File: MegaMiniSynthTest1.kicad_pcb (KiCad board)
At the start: 2 copper layers, 73.5 x 56.9 mm, 35 parts, among them K1 CONN_3, P4 DIN_5, U1 MC33269, U2 TLE2426, U3 PCA9685

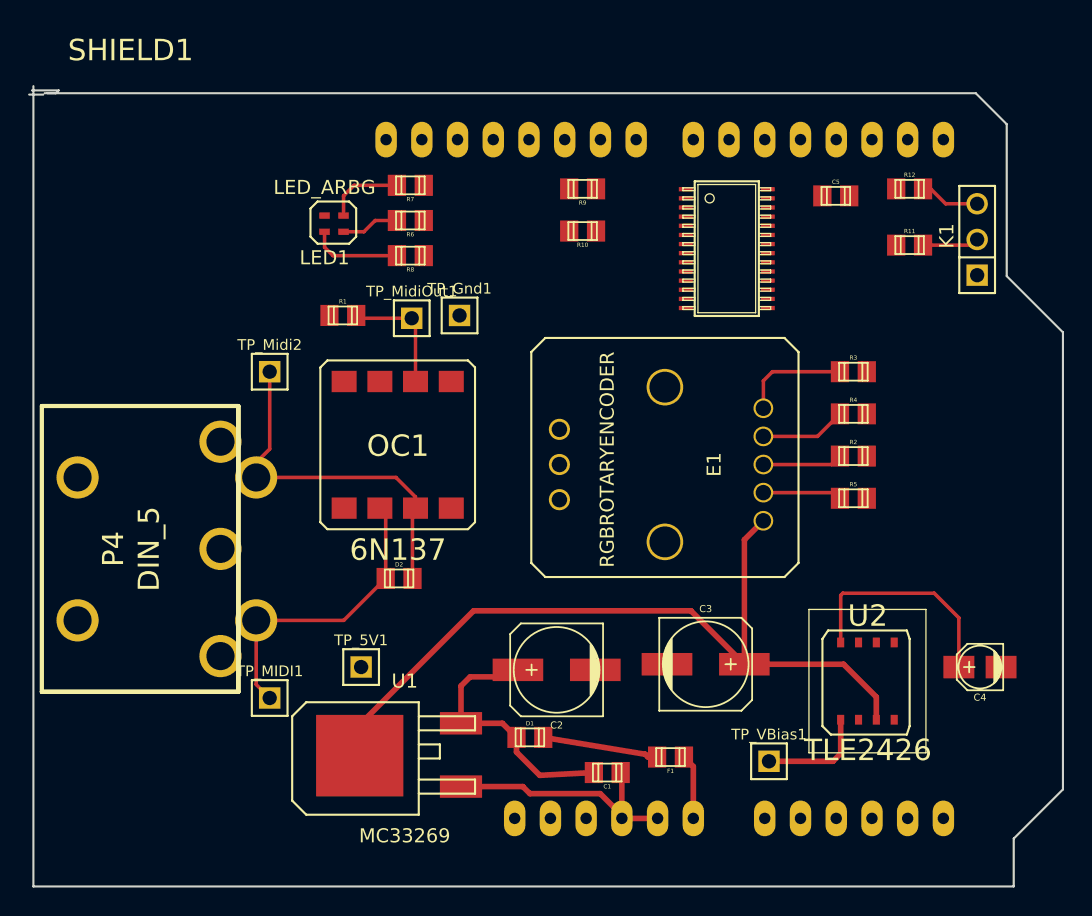
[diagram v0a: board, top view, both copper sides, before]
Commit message: Moved to new KiCad Version
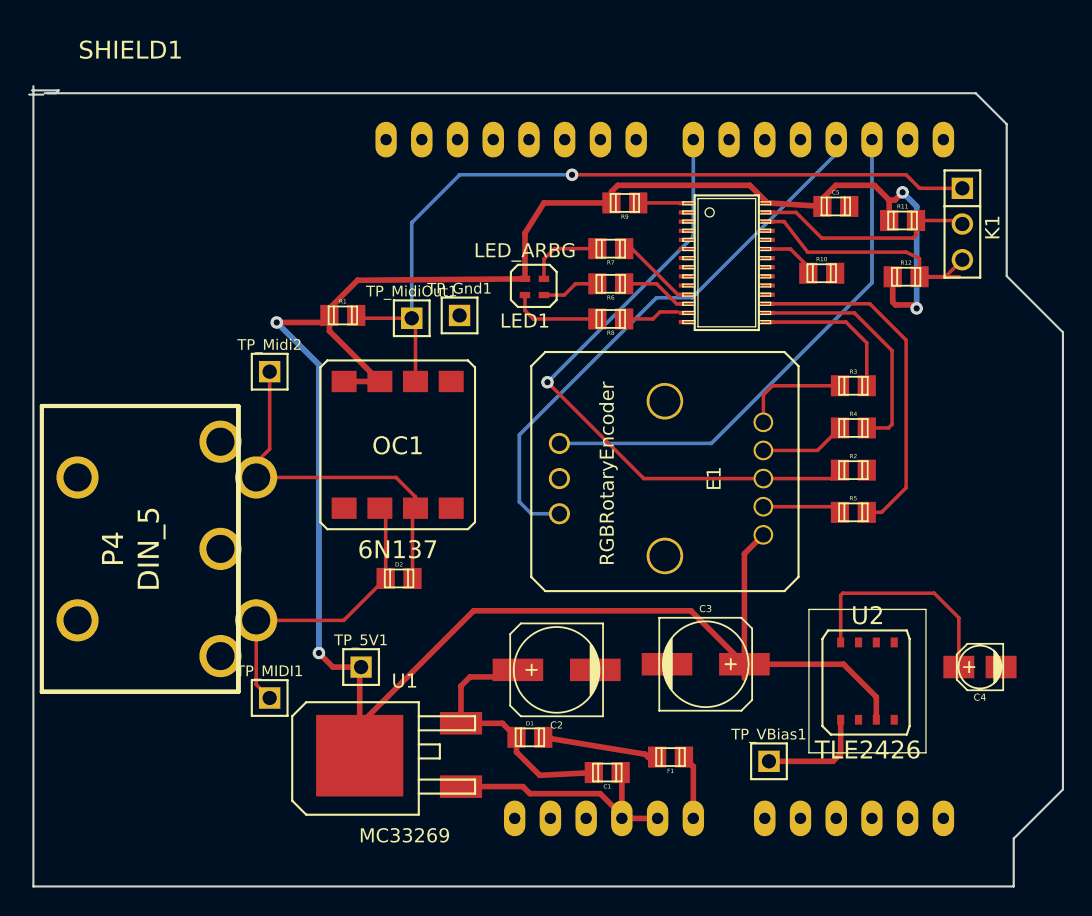
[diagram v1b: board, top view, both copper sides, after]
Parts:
- E1: value RGBROTARYENCODER -> RGBRotaryEncoder
- moved R10 17.3 mm to (134.8, 39.0), turned to 0 degrees
- moved LED1 14.9 mm to (113.7, 39.4)
- moved R6 14.9 mm to (119.8, 39.8)
- moved R7 14.9 mm to (119.8, 37.2)
- moved R8 14.9 mm to (119.8, 42.2)
- moved R12 6.25 mm to (140.8, 39.2)
- moved R9 3.16 mm to (120.8, 34.0)
- moved R11 1.82 mm to (140.5, 35.2)
- moved K1 1.52 mm to (144.8, 35.5), turned to 270 degrees
- moved E1 1.00 mm to (116.1, 53.6)
- moved R2 1.00 mm to (137.0, 53.0)
- moved R3 1.00 mm to (137.0, 47.0)
- moved R4 1.00 mm to (137.0, 50.0)
- moved R5 1.00 mm to (137.0, 56.0)
- moved U3 1.00 mm to (128.0, 38.2)
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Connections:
- P4 pad 1: (no net) -> Net-(P4-Pad1)
- P4 pad 2: (no net) -> Net-(P4-Pad2)
- P4 pad 3: (no net) -> Net-(P4-Pad3)
- R3 pad 1: N-0000027 -> Net-(R3-Pad1)
- R5 pad 1: N-0000029 -> Net-(R5-Pad1)
- R6 pad 2: N-0000020 -> Net-(R6-Pad2)
- R7 pad 2: N-0000021 -> Net-(R7-Pad2)
- SHIELD1 pad 0: (no net) -> Net-(SHIELD1-Pad0)
- SHIELD1 pad 1: (no net) -> Net-(SHIELD1-Pad1)
- SHIELD1 pad 10: (no net) -> Net-(SHIELD1-Pad10)
- SHIELD1 pad 11: (no net) -> Net-(SHIELD1-Pad11)
- SHIELD1 pad 12: (no net) -> Net-(SHIELD1-Pad12)
- SHIELD1 pad 13: (no net) -> Net-(SHIELD1-Pad13)
- SHIELD1 pad 3V3: (no net) -> Net-(SHIELD1-Pad3V3)
- SHIELD1 pad 4: (no net) -> Net-(SHIELD1-Pad4)
- SHIELD1 pad 5: (no net) -> Net-(SHIELD1-Pad5)
- SHIELD1 pad 5V: (no net) -> Net-(SHIELD1-Pad5V)
- SHIELD1 pad 6: (no net) -> Net-(SHIELD1-Pad6)
- SHIELD1 pad 8: (no net) -> Net-(SHIELD1-Pad8)
- SHIELD1 pad 9: (no net) -> Net-(SHIELD1-Pad9)
- SHIELD1 pad AD0: (no net) -> Net-(SHIELD1-PadAD0)
- SHIELD1 pad AD1: (no net) -> Net-(SHIELD1-PadAD1)
- SHIELD1 pad AD2: (no net) -> Net-(SHIELD1-PadAD2)
- SHIELD1 pad AD3: (no net) -> Net-(SHIELD1-PadAD3)
- SHIELD1 pad AD4: (no net) -> Net-(SHIELD1-PadAD4)
- SHIELD1 pad AD5: (no net) -> Net-(SHIELD1-PadAD5)
- SHIELD1 pad AREF: (no net) -> Net-(SHIELD1-PadAREF)
- SHIELD1 pad GND3: (no net) -> Net-(SHIELD1-PadGND3)
- SHIELD1 pad RST: (no net) -> Net-(SHIELD1-PadRST)
- U3 pad 10: (no net) -> Net-(U3-Pad10)
- U3 pad 11: N-0000020 -> Net-(R7-Pad2)
- U3 pad 12: N-0000021 -> Net-(R6-Pad2)
- U3 pad 15: N-0000029 -> Net-(R3-Pad1)
- U3 pad 17: N-0000027 -> Net-(R5-Pad1)
- U3 pad 18: (no net) -> Net-(U3-Pad18)
- U3 pad 19: (no net) -> Net-(U3-Pad19)
- U3 pad 20: (no net) -> Net-(U3-Pad20)
- U3 pad 21: (no net) -> Net-(U3-Pad21)
- U3 pad 22: (no net) -> Net-(U3-Pad22)
- U3 pad 6: (no net) -> Net-(U3-Pad6)
- U3 pad 7: (no net) -> Net-(U3-Pad7)
- U3 pad 8: (no net) -> Net-(U3-Pad8)
- U3 pad 9: (no net) -> Net-(U3-Pad9)
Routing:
- net +5V: track 57.2 -> 167.8 mm, vias 0 -> 4
- net Serial2: track 8.64 -> 56.4 mm, vias 0 -> 1
- net Arduino3: track 0.00 -> 38.8 mm
- net Arduino7: track 5.70 -> 44.4 mm, vias 0 -> 1
- net Arduino2: track 0.00 -> 36.1 mm
- net Net-(R5-Pad1): track 0.00 -> 24.9 mm
- net Net-(R4-Pad1): track 0.00 -> 17.1 mm
- net SCL: track 4.29 -> 19.9 mm
- net SDA: track 4.01 -> 16.2 mm
- net Net-(R3-Pad1): track 0.00 -> 10.7 mm
- net Net-(R7-Pad2): track 0.00 -> 5.74 mm
- net Net-(R6-Pad2): track 0.00 -> 4.97 mm
- net Net-(R8-Pad2): track 0.00 -> 4.00 mm
- net Net-(R10-Pad2): track 0.00 -> 3.86 mm
- net Net-(R9-Pad2): track 0.00 -> 3.39 mm

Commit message: Board Layout basically done
Added bypass cap for PWM driver
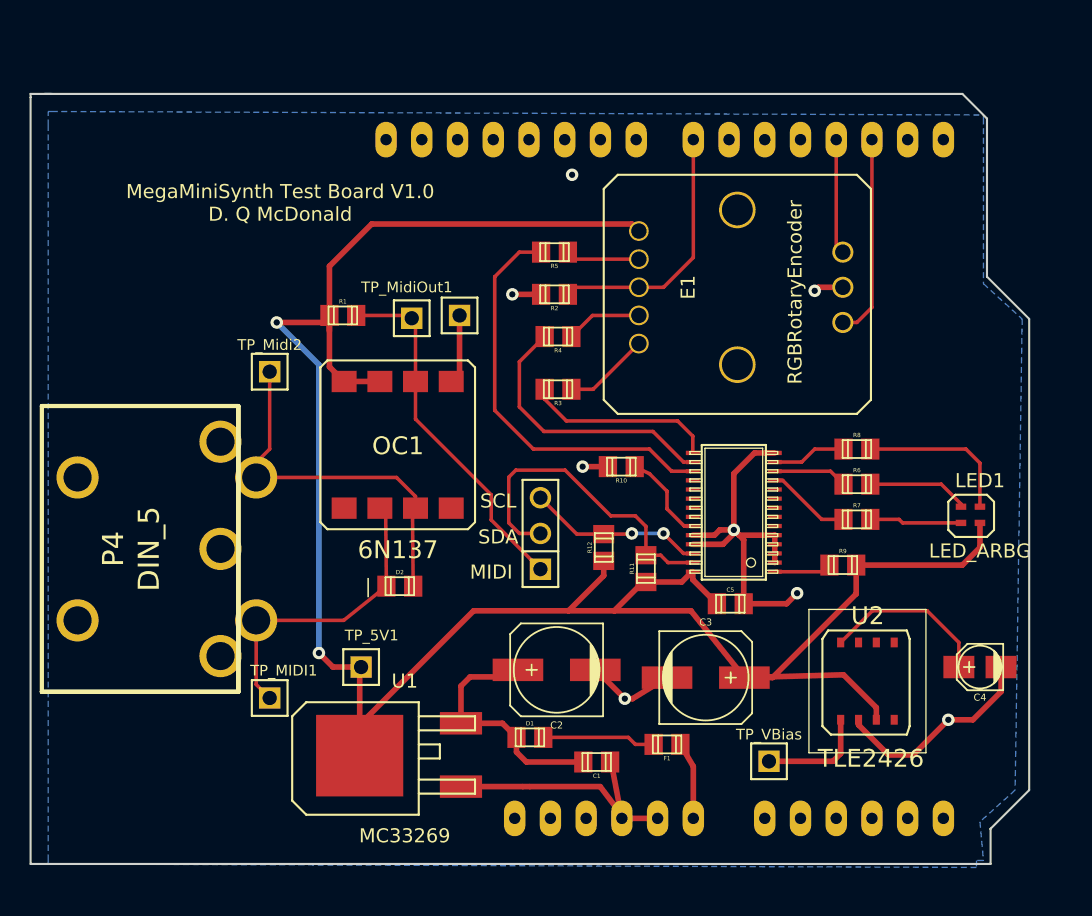
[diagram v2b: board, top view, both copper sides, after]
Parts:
- ?: renamed from SHIELD1; value ARDUINO_SHIELD -> (none)
- ?: renamed from K1; value CONN_3 -> (none)
- TP_5V1: value TP_5V -> (none)
- TP_MIDI1, TP_Midi2, TP_MidiOut1: value CONN_1 -> (none)
- TP_VBias: renamed from TP_VBias1; value Tl_VBias -> (none)
- moved ? 37.2 mm to (114.8, 57.5), turned to 90 degrees
- moved LED1 36.7 mm to (146.0, 56.8), turned to 0 degrees
- moved R11 30.8 mm to (122.2, 60.0), turned to 90 degrees
- moved R9 30.1 mm to (136.2, 59.8), turned to 0 degrees
- moved C5 29.2 mm to (128.2, 62.5)
- moved R12 28.9 mm to (119.2, 58.5), turned to 90 degrees
- moved R5 28.2 mm to (115.8, 37.5), turned to 180 degrees
- moved R7 26.0 mm to (137.2, 56.5), turned to 0 degrees
- moved R2 24.7 mm to (115.8, 40.5), turned to 180 degrees
- moved E1 24.3 mm to (136.2, 40.0), turned to 90 degrees
- moved R6 22.6 mm to (137.2, 54.0), turned to 0 degrees
- moved R4 22.0 mm to (116.0, 43.5), turned to 180 degrees
- moved R3 21.0 mm to (116.0, 47.2), turned to 180 degrees
- moved R10 19.8 mm to (120.5, 52.8), turned to 180 degrees
- moved R8 19.8 mm to (137.2, 51.5), turned to 0 degrees
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- renumbered TP_Gnd1 to ?
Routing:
- net GND: track 18.3 -> 80.6 mm, vias 0 -> 7
- net Serial2: track 56.4 -> 25.9 mm, vias 1 -> 0
- net Arduino3: track 38.8 -> 8.34 mm
- net Arduino7: track 44.4 -> 18.4 mm, vias 1 -> 0
- net Arduino2: track 36.1 -> 14.4 mm
- net +5V: track 167.8 -> 158.4 mm, vias 4 -> 2
- net SCL: track 19.9 -> 12.5 mm, vias 0 -> 2
- net SDA: track 16.2 -> 23.0 mm
- net Net-(LED1-Pad3): track 6.50 -> 11.3 mm
- net Net-(R5-Pad1): track 24.9 -> 29.4 mm
- net Net-(C4-Pad1): track 16.0 -> 12.0 mm
- net Net-(LED1-Pad2): track 4.13 -> 7.23 mm
- net Net-(R3-Pad1): track 10.7 -> 13.5 mm
- net Net-(R10-Pad2): track 3.86 -> 6.52 mm
- net Net-(R4-Pad1): track 17.1 -> 19.7 mm
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- added copper zone on B.Cu, net GND
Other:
- board size 73.5 x 56.9 mm -> 71 x 54.8 mm
- board text added: "MIDI"
- board text added: "MegaMiniSynth Test Board V1.0 D. Q McDonald"
- board text added: "SCL"
- board text added: "SDA"
- board text added: "|"

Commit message: Final version 1.0 as sent to OSHPark
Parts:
- added ?: , DQM:MMS_LOGO, F.Cu at (87.0, 38.2)
- LED1: footprint SMDRGBLED -> DQM:SMDRGBLED
- OC1: footprint 6N137 -> DQM:6N137
- U2: footprint TLE2426 -> DQM:TLE2426
